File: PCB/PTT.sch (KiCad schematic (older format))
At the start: 16 parts, among them Q7 2N3904, U8 LM324N

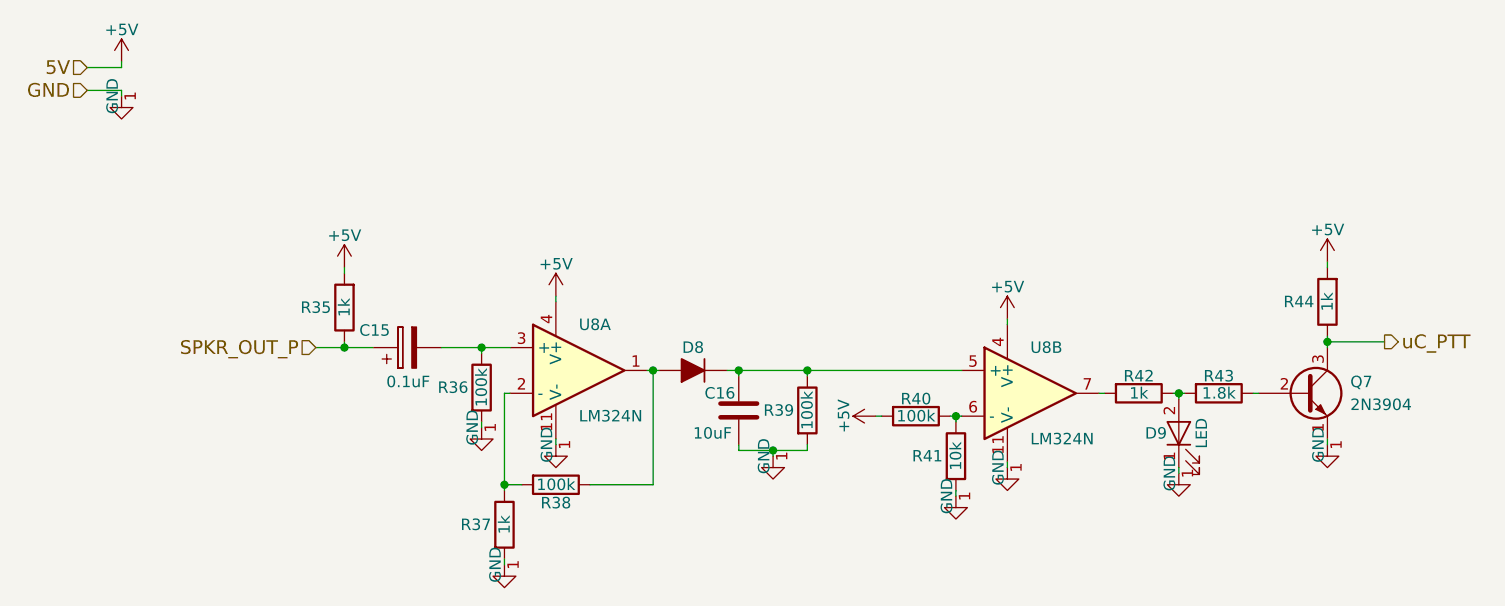
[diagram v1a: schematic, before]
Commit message: Added PCB layout
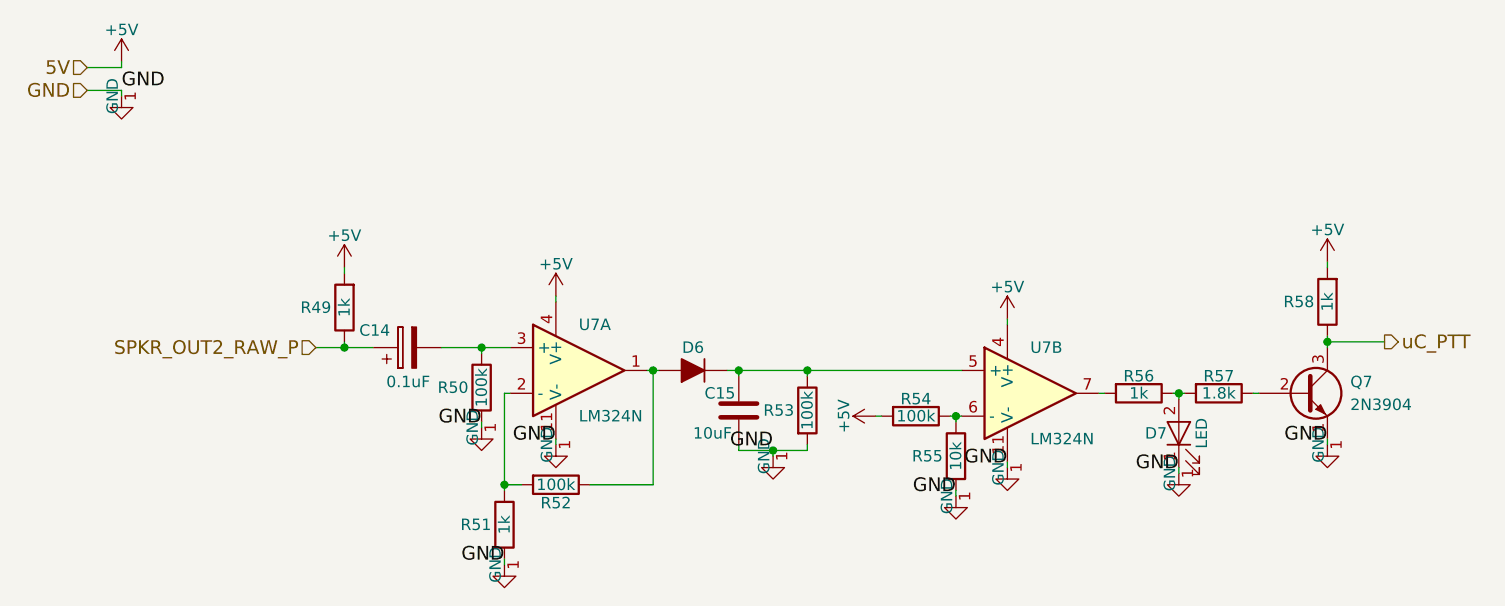
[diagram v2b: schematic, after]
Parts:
- C14: renamed from C15; footprint (none) -> Capacitors_THT:CP_Radial_D5.0mm_P2.00mm
- C15: renamed from C16; footprint (none) -> Capacitors_SMD:C_0603_HandSoldering
- D6: renamed from D8; footprint (none) -> Diodes_SMD:D_SOD-323_HandSoldering
- D7: renamed from D9; footprint (none) -> LEDs:LED_0805_HandSoldering
- Q7: footprint (none) -> TO_SOT_Packages_THT:TO-92_Molded_Narrow
- R49: renamed from R35; footprint (none) -> Resistors_SMD:R_0603_HandSoldering
- R50: renamed from R36; footprint (none) -> Resistors_SMD:R_0603_HandSoldering
- R51: renamed from R37; footprint (none) -> Resistors_SMD:R_0603_HandSoldering
- R52: renamed from R38; footprint (none) -> Resistors_SMD:R_0603_HandSoldering
- R53: renamed from R39; footprint (none) -> Resistors_SMD:R_0603_HandSoldering
- R54: renamed from R40; footprint (none) -> Resistors_SMD:R_0603_HandSoldering
- R55: renamed from R41; footprint (none) -> Resistors_SMD:R_0603_HandSoldering
- R56: renamed from R42; footprint (none) -> Resistors_SMD:R_0603_HandSoldering
- R57: renamed from R43; footprint (none) -> Resistors_SMD:R_0603_HandSoldering
- R58: renamed from R44; footprint (none) -> Resistors_SMD:R_0603_HandSoldering
- U7: renamed from U8; footprint (none) -> SMD_Packages:SOIC-14_N
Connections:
- net GND: now also C15.2, D7.1 (K), Q7.1 (E), R50.2, R51.2, R53.2, R55.2, U7.11 (V-), U7.11 (V-)
- net SPKR_OUT_P renamed SPKR_OUT2_RAW_P
